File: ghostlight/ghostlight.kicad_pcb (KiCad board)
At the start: 2 copper layers, 25 x 25 mm, 12 parts, among them IC1 STM32C011J4M6, IC2 MCP1700T-3302E_TT, IC3 LP5817DRLR, J1 Conn_01x08

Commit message: change in schematic
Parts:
- moved C4 3.54 mm to (153.0, 92.0), turned to 180 degrees
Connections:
- IC1 pad 5: unconnected-(IC1-PA11[PA9]/PA8-Pad5) -> LIVE
- IC1 pad 6: unconnected-(IC1-PA12[PA10]-Pad6) -> I2C_ERR
- J1 pad 2: unconnected-(J1-Pin_2-Pad2) -> SCK
- J1 pad 3: SCK -> ST_LINK_SWDIO
- J1 pad 4: ST_LINK_SWDIO -> I2C_ERR
- J1 pad 5: ST_LINK_RST/RST -> LIVE
- J1 pad 6: unconnected-(J1-Pin_6-Pad6) -> ST_LINK_RST/RST
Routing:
- net LIVE: track 0.00 -> 8.77 mm
- net I2C_ERR: track 0.00 -> 5.85 mm
- net 3.3V: track 36.1 -> 32.3 mm, vias 4 -> 2
- net Net-(IC3-OUT0): track 3.89 -> 7.62 mm
- net SCK: track 26.3 -> 23.0 mm
- net ST_LINK_SWDIO: track 5.33 -> 8.16 mm
- net Net-(IC3-OUT1): track 6.66 -> 4.45 mm
- net ST_LINK_RST/RST: track 14.2 -> 16.2 mm
- net GND: track 10.4 -> 9.49 mm
- net Net-(IC3-OUT2): track 10.1 -> 9.54 mm

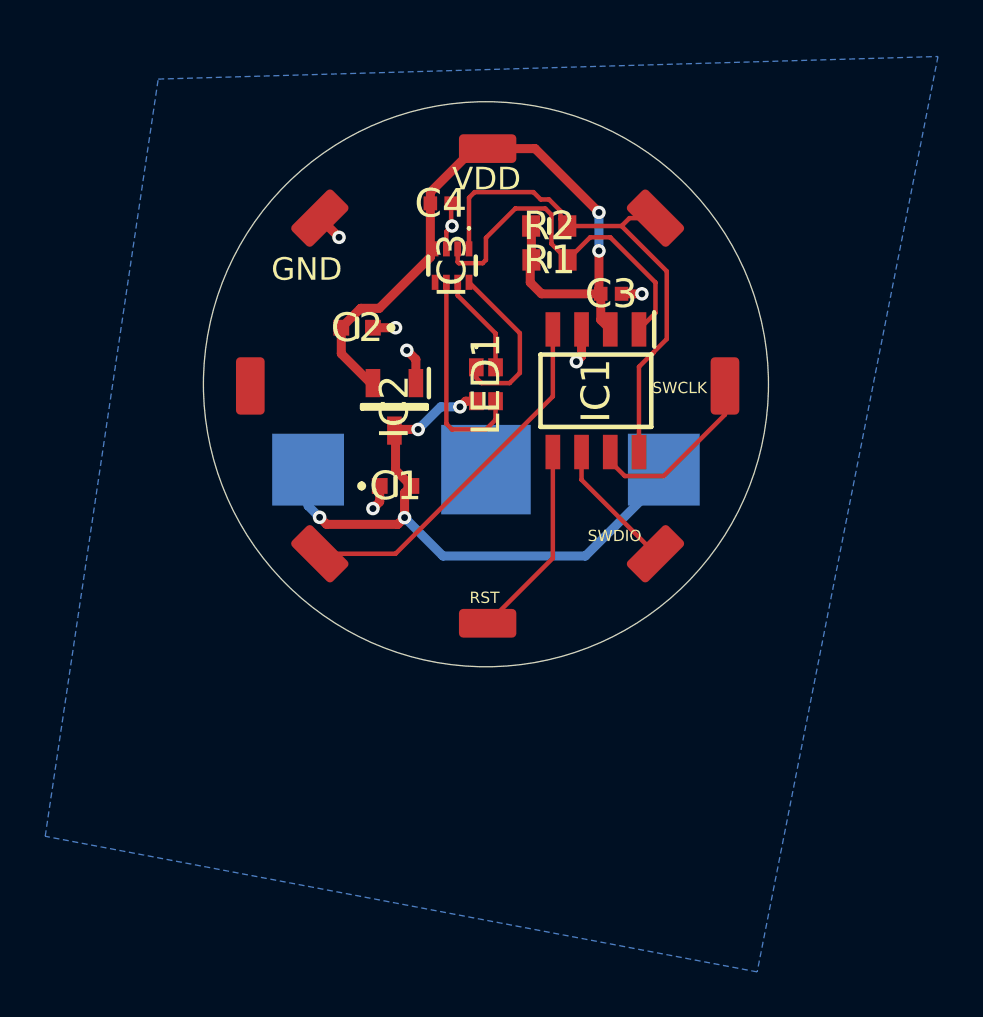
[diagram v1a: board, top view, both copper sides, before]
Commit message: Add Test Points
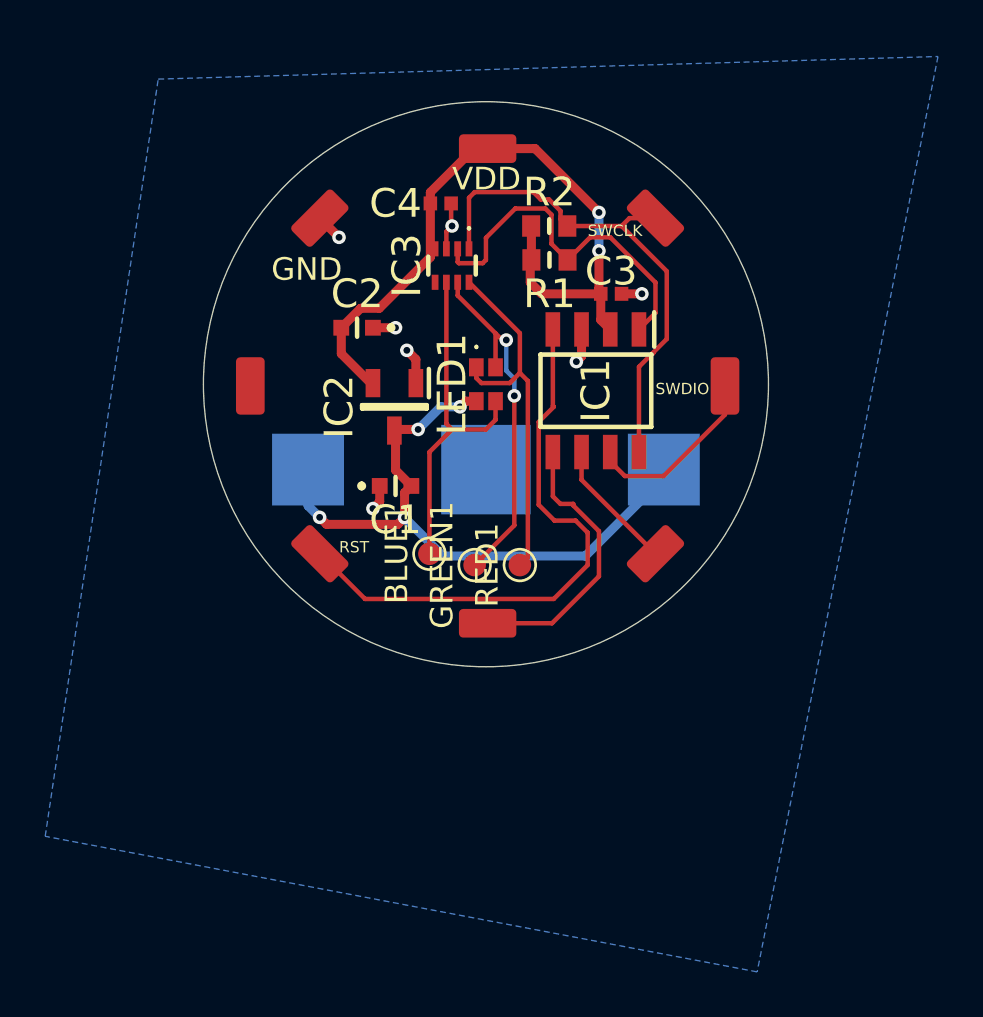
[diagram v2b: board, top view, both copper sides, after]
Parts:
- added BLUE1: TP_B, TestPoint:TestPoint_Pad_D1.0mm, F.Cu at (152.5, 107.5)
- added GREEN1: TP_G, TestPoint:TestPoint_Pad_D1.0mm, F.Cu at (154.5, 108.0)
- added RED1: TP_R, TestPoint:TestPoint_Pad_D1.0mm, F.Cu at (156.5, 108.0)
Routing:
- net Net-(IC3-OUT1): track 4.45 -> 15.9 mm, vias 0 -> 2
- net ST_LINK_RST/RST: track 16.2 -> 25.5 mm
- net Net-(IC3-OUT0): track 7.62 -> 16.4 mm
- net Net-(IC3-OUT2): track 9.54 -> 15.5 mm
- net LIVE: track 8.77 -> 12.5 mm

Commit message: Add new battery holder
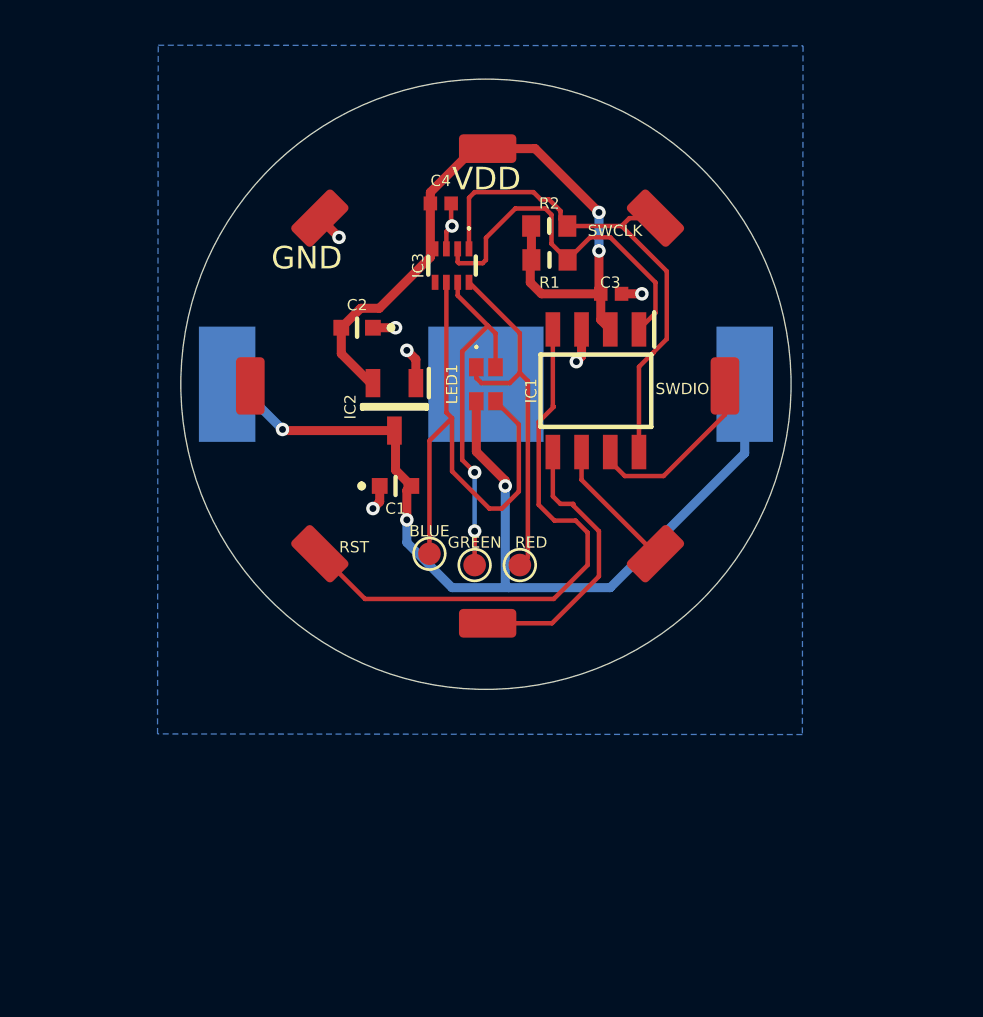
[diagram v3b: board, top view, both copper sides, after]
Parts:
- BT1: footprint SamacSys_Parts:3000 -> custom_ring:Battery_Holder_Lynx_CR2032
- moved BT1 4.50 mm to (155.0, 100.0)
- renumbered BLUE1 to BLUE, GREEN1 to GREEN, RED1 to RED
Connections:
- BT1 pad 1: V_BAT -> GND
- BT1 pad 3: GND -> V_BAT
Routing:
- net V_BAT: track 28.7 -> 44.4 mm, vias 4 -> 3
- net Net-(IC3-OUT2): track 15.5 -> 23.3 mm
- net GND: track 9.49 -> 13.3 mm
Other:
- board size 25 x 25 mm -> 27 x 27 mm
